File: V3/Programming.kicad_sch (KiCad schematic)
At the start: 10 parts, among them J3 RRC3_In, J4 I2C_Interface_Male, J5 USB_B_Micro, Q4 MMBT2222, Q5 MMBT2222, U8 CP2102N-A01-GQFN28

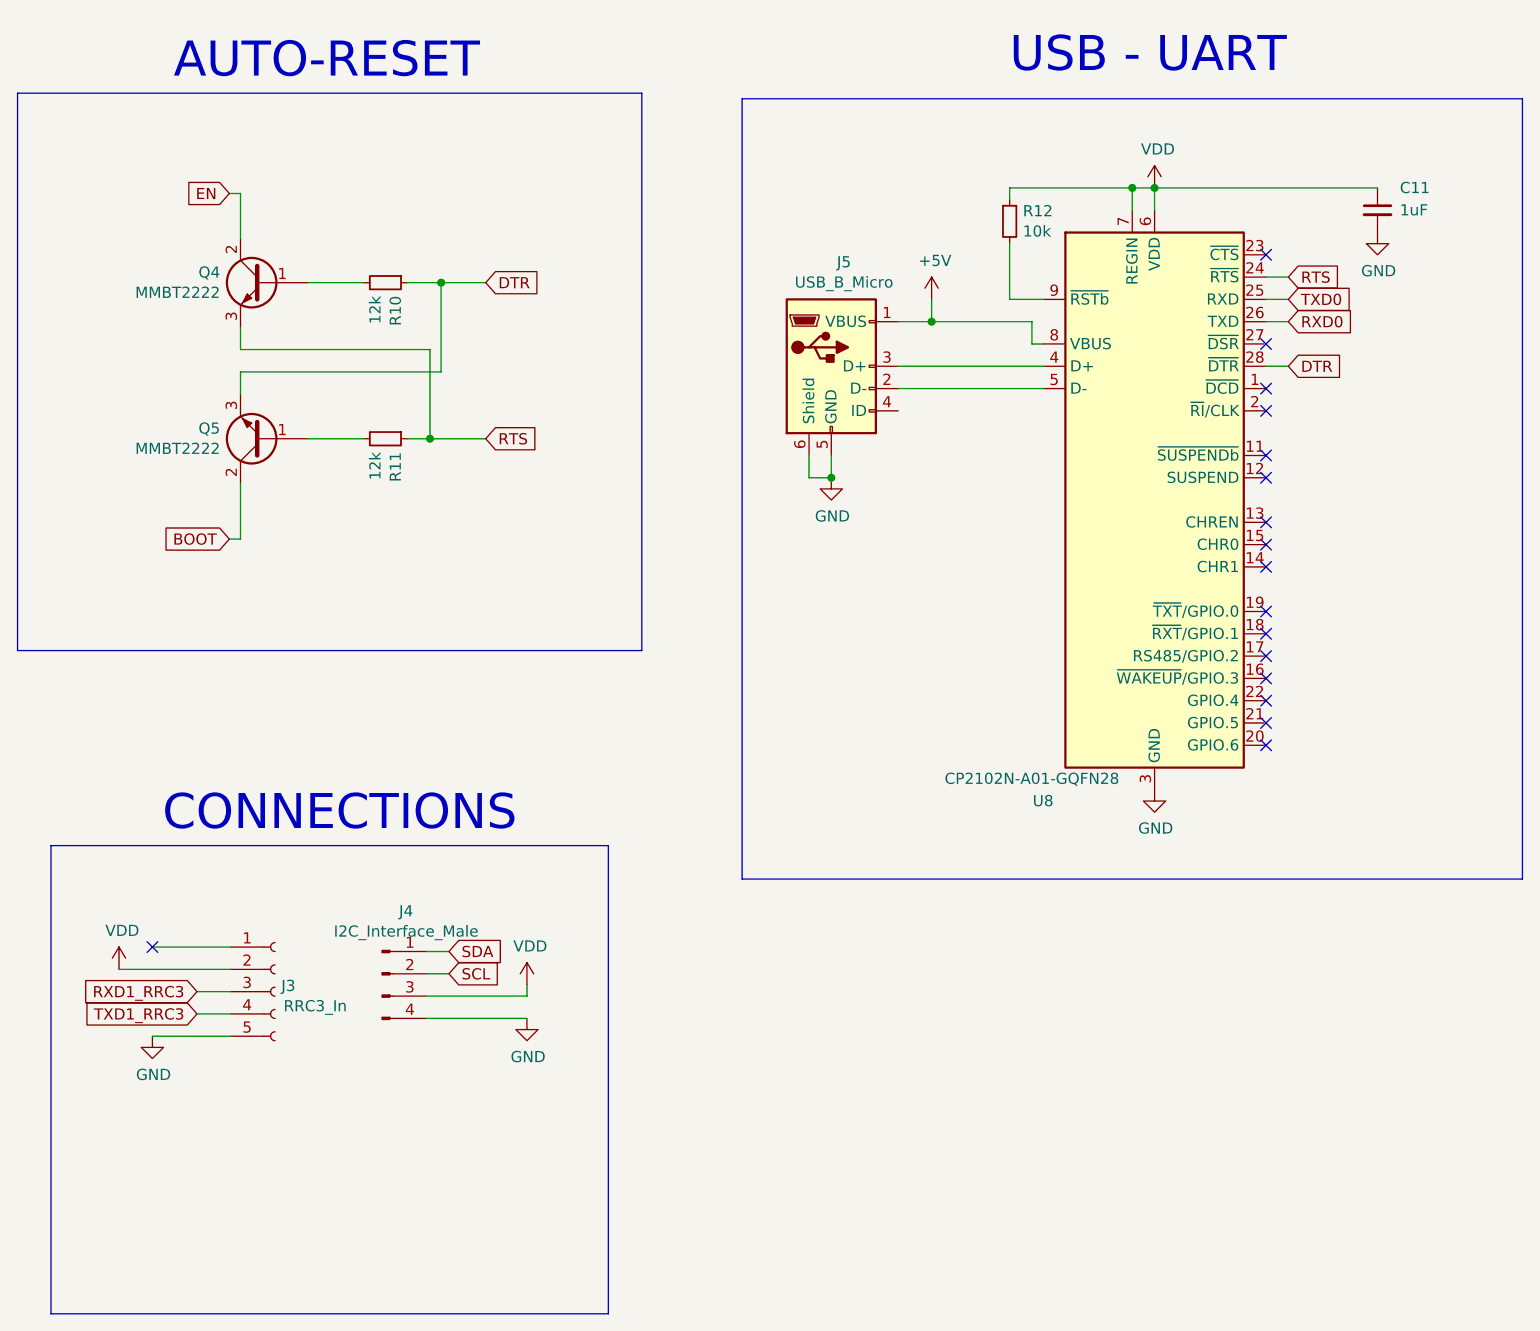
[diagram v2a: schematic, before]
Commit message: New parts placed and routed
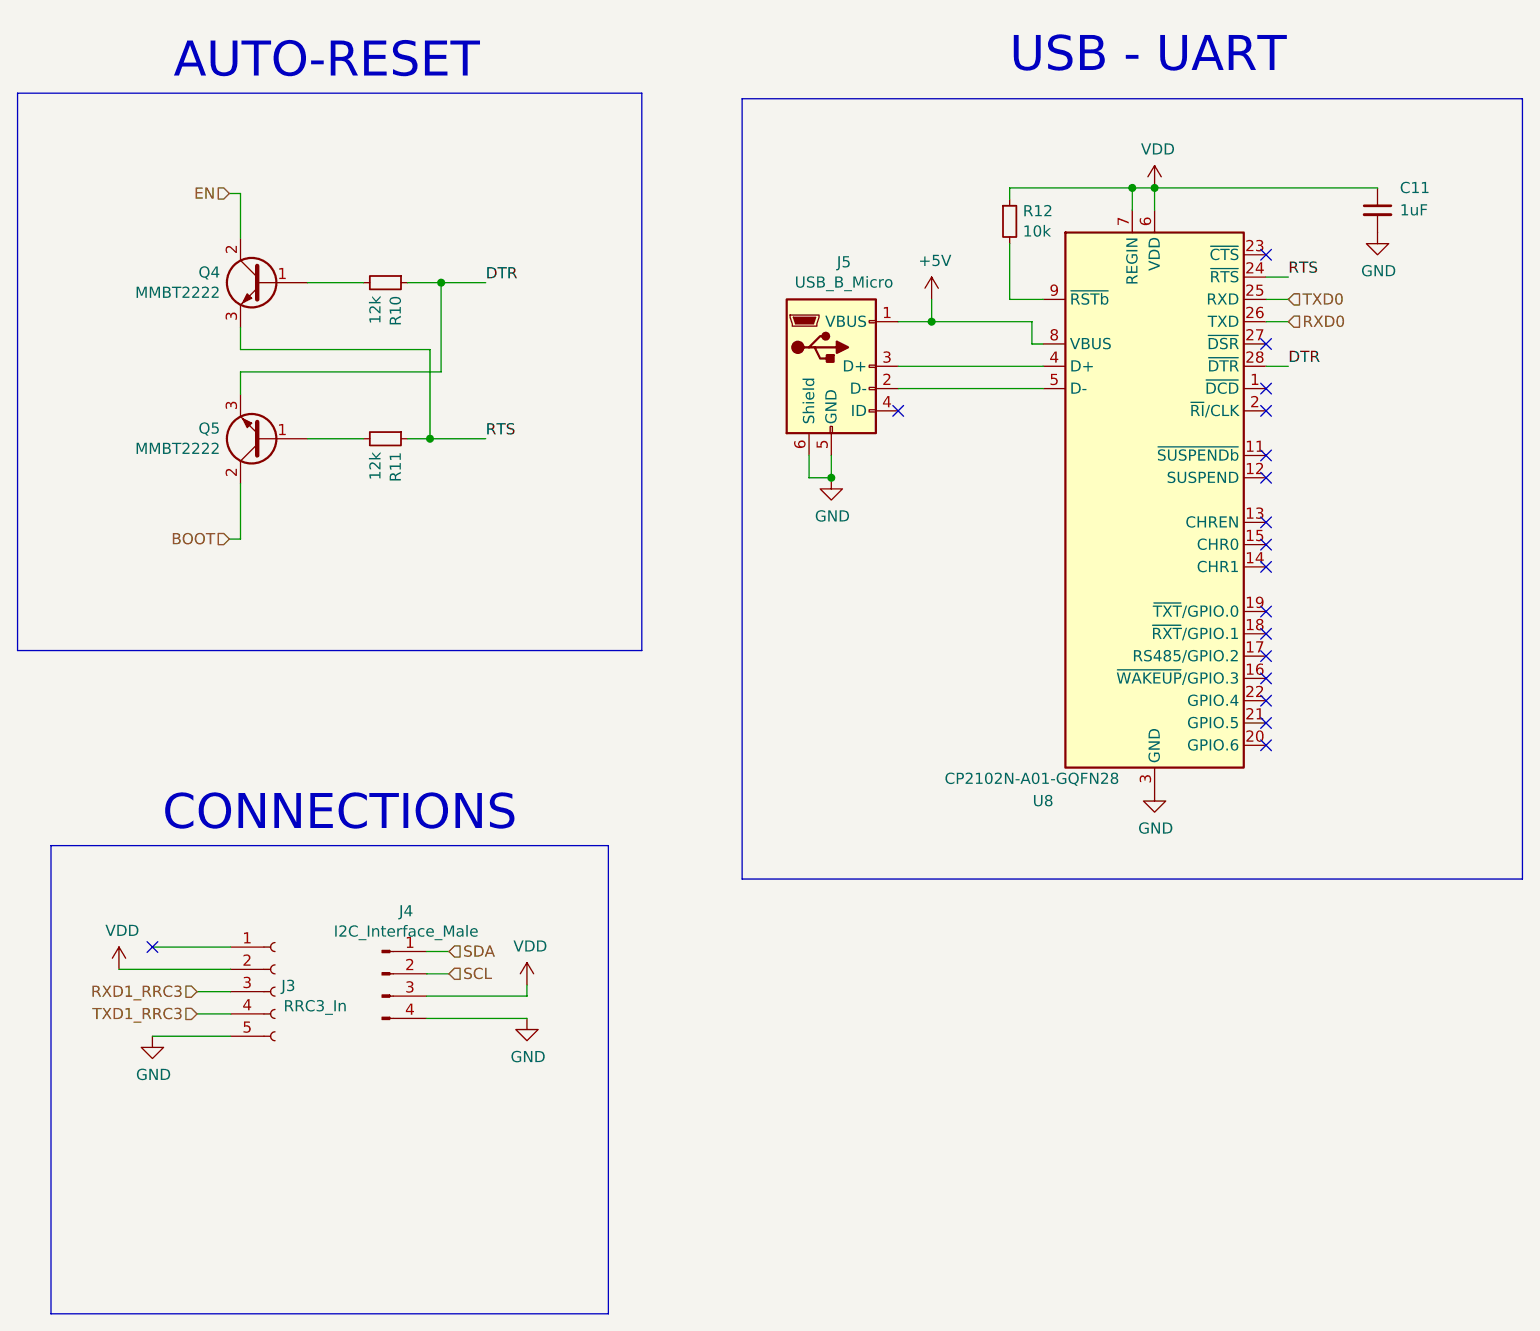
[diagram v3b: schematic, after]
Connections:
- no-connect marks 17 -> 18
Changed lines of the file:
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@@
   (no_connect (at 173.355 81.915))
   (no_connect (at 173.355 92.075))
+  (no_connect (at 131.445 64.135))
   (no_connect (at 173.355 69.215))
   (no_connect (at 173.355 61.595))
@@
     (effects (font (size 3.9878 3.9878)) (justify left bottom))
   )
-  (global_label "SCL" (shape input) (at 80.264 128.27 0) (fields_autoplaced)
-    (effects (font (size 1.27 1.27)) (justify left))
-    (property "Intersheet References" "${INTERSHEET_REFS}" (id 0) (at -106.426 48.26 0)
-      (effects (font (size 1.27 1.27)) hide)
-    )
-  )
-  (global_label "RXD1_RRC3" (shape input) (at 51.562 130.302 180) (fields_autoplaced)
-    (effects (font (size 1.27 1.27)) (justify right))
-    (property "Intersheet References" "${INTERSHEET_REFS}" (id 0) (at -105.918 70.612 0)
-      (effects (font (size 1.27 1.27)) hide)
-    )
-  )
-  (global_label "RTS" (shape input) (at 84.455 67.31 0) (fields_autoplaced)
-    (effects (font (size 1.27 1.27)) (justify left))
-    (property "Intersheet References" "${INTERSHEET_REFS}" (id 0) (at -280.035 -152.4 0)
-      (effects (font (size 1.27 1.27)) hide)
-    )
-  )
-  (global_label "DTR" (shape input) (at 175.895 59.055 0) (fields_autoplaced)
-    (effects (font (size 1.27 1.27)) (justify left))
-    (property "Intersheet References" "${INTERSHEET_REFS}" (id 0) (at -27.305 -151.765 0)
-      (effects (font (size 1.27 1.27)) hide)
-    )
-  )
-  (global_label "BOOT" (shape input) (at 55.245 78.74 180) (fields_autoplaced)
-    (effects (font (size 1.27 1.27)) (justify right))
-    (property "Intersheet References" "${INTERSHEET_REFS}" (id 0) (at -280.035 -152.4 0)
-      (effects (font (size 1.27 1.27)) hide)
-    )
-  )
-  (global_label "EN" (shape input) (at 55.245 39.37 180) (fields_autoplaced)
-    (effects (font (size 1.27 1.27)) (justify right))
-    (property "Intersheet References" "${INTERSHEET_REFS}" (id 0) (at -280.035 -152.4 0)
-      (effects (font (size 1.27 1.27)) hide)
-    )
-  )
-  (global_label "TXD0" (shape input) (at 175.895 51.435 0) (fields_autoplaced)
-    (effects (font (size 1.27 1.27)) (justify left))
-    (property "Intersheet References" "${INTERSHEET_REFS}" (id 0) (at -27.305 -151.765 0)
-      (effects (font (size 1.27 1.27)) hide)
-    )
-  )
-  (global_label "RXD0" (shape input) (at 175.895 53.975 0) (fields_autoplaced)
-    (effects (font (size 1.27 1.27)) (justify left))
-    (property "Intersheet References" "${INTERSHEET_REFS}" (id 0) (at -27.305 -151.765 0)
-      (effects (font (size 1.27 1.27)) hide)
-    )
-  )
-  (global_label "RTS" (shape input) (at 175.895 48.895 0) (fields_autoplaced)
-    (effects (font (size 1.27 1.27)) (justify left))
-    (property "Intersheet References" "${INTERSHEET_REFS}" (id 0) (at -27.305 -151.765 0)
-      (effects (font (size 1.27 1.27)) hide)
-    )
-  )
-  (global_label "DTR" (shape input) (at 84.455 49.53 0) (fields_autoplaced)
-    (effects (font (size 1.27 1.27)) (justify left))
-    (property "Intersheet References" "${INTERSHEET_REFS}" (id 0) (at -280.035 -152.4 0)
-      (effects (font (size 1.27 1.27)) hide)
-    )
-  )
-  (global_label "TXD1_RRC3" (shape input) (at 51.562 132.842 180) (fields_autoplaced)
-    (effects (font (size 1.27 1.27)) (justify right))
-    (property "Intersheet References" "${INTERSHEET_REFS}" (id 0) (at -105.918 70.612 0)
-      (effects (font (size 1.27 1.27)) hide)
-    )
-  )
-  (global_label "SDA" (shape input) (at 80.264 125.73 0) (fields_autoplaced)
-    (effects (font (size 1.27 1.27)) (justify left))
-    (property "Intersheet References" "${INTERSHEET_REFS}" (id 0) (at -106.426 48.26 0)
-      (effects (font (size 1.27 1.27)) hide)
-    )
+  (label "RTS" (at 175.895 48.895 0)
+    (effects (font (size 1.27 1.27)) (justify left bottom))
+  )
+  (label "DTR" (at 84.455 49.53 0)
+    (effects (font (size 1.27 1.27)) (justify left bottom))
+  )
+  (label "DTR" (at 175.895 59.055 0)
+    (effects (font (size 1.27 1.27)) (justify left bottom))
+  )
+  (label "RTS" (at 84.455 67.31 0)
+    (effects (font (size 1.27 1.27)) (justify left bottom))
+  )
+  (hierarchical_label "BOOT" (shape input) (at 55.245 78.74 180)
+    (effects (font (size 1.27 1.27)) (justify right))
+  )
+  (hierarchical_label "SDA" (shape input) (at 80.264 125.73 0)
+    (effects (font (size 1.27 1.27)) (justify left))
+  )
+  (hierarchical_label "TXD0" (shape input) (at 175.895 51.435 0)
+    (effects (font (size 1.27 1.27)) (justify left))
+  )
+  (hierarchical_label "TXD1_RRC3" (shape input) (at 51.562 132.842 180)
+    (effects (font (size 1.27 1.27)) (justify right))
+  )
+  (hierarchical_label "RXD0" (shape input) (at 175.895 53.975 0)
+    (effects (font (size 1.27 1.27)) (justify left))
+  )
+  (hierarchical_label "RXD1_RRC3" (shape input) (at 51.562 130.302 180)
+    (effects (font (size 1.27 1.27)) (justify right))
+  )
+  (hierarchical_label "SCL" (shape input) (at 80.264 128.27 0)
+    (effects (font (size 1.27 1.27)) (justify left))
+  )
+  (hierarchical_label "EN" (shape input) (at 55.245 39.37 180)
+    (effects (font (size 1.27 1.27)) (justify right))
   )
   (symbol (lib_id "power:VDD") (at 42.672 127.762 0) (unit 1)
